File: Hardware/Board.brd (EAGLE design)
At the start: 170.2 x 111.2 mm, 103 parts, among them IC1 BD5229G-TR, IC4 XC6220A331MR-G, J1 FH34SRJ-24S-0.5SH_99_, J2 SAMACSYS_PARTS_USB4110-GF-A, J3 QWIIC_RIGHT_ANGLE, J4 112A-TAAR-R03_ATTEND, Q1 20V/4.2A/52mΩ/1.4W, Q2 20V/4.2A/52mΩ/1.4W, Q3 SI1308EDL-T1-GE3, U1 W25Q512JVEIQ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

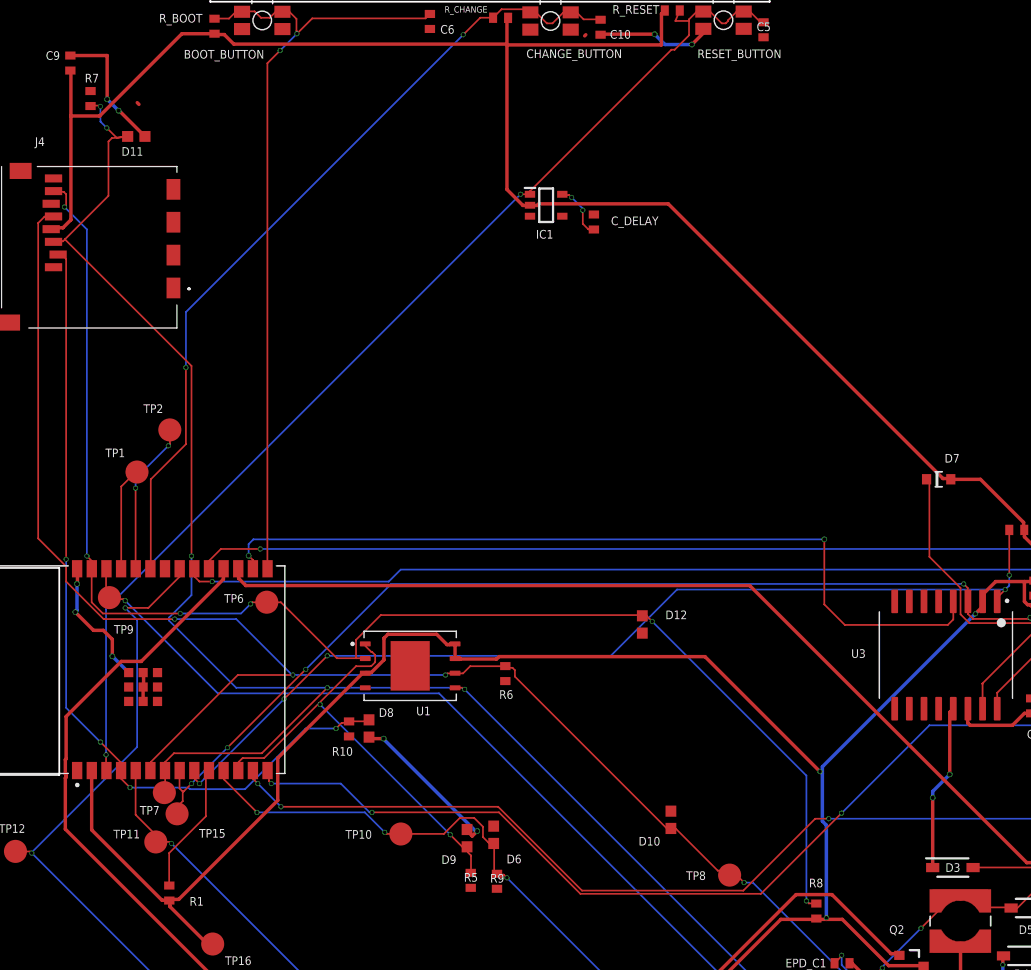
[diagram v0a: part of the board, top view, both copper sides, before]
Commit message: Remaining exploded view and manufacturing
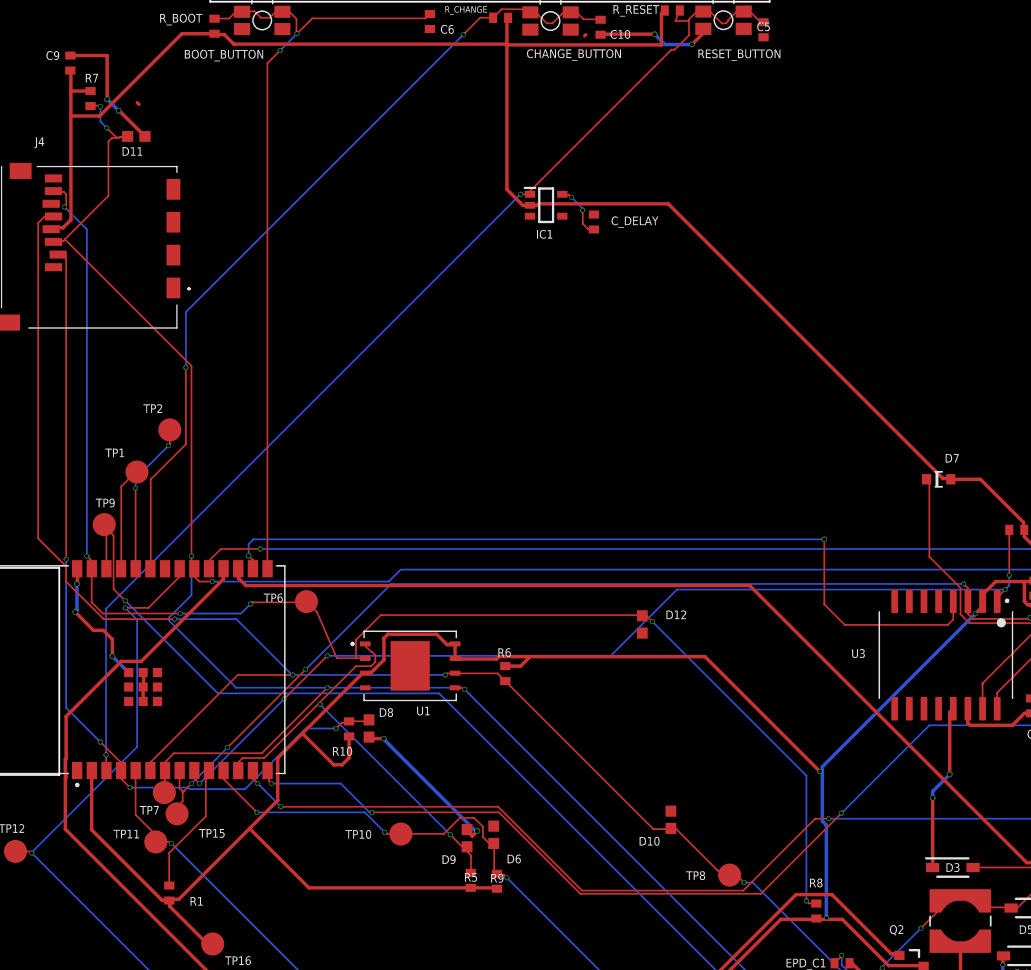
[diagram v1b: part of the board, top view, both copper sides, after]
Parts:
- R1: value (none) -> 10K
- moved TP9 6.35 mm to (10.3, 64.9)
- moved TP6 3.44 mm to (27.8, 58.2)
- turned R6 to 90 degrees
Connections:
- removed net N$26: R7.2
- removed net N$27: R6.2
- removed net N$28: R5.2
- removed net N$29: R9.2
- removed net N$30: R10.2
- net 3V3: now also R10.2, R5.2, R6.2, R7.2, R9.2
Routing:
- net 3V3: track 418.9 -> 454.0 mm
- net EPD_BUSY: track 99.3 -> 106.4 mm
- net MISO: track 123.3 -> 124.3 mm
- net SCK: track 148.0 -> 147.2 mm

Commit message: FInal version of files. Remaining gerbers
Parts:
- R_CHANGE: value (none) -> 10K
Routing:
- net GND: vias 18 -> 40
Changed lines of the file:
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@@
 <layer number="17" name="Pads" color="2" fill="1" visible="yes" active="yes"/>
 <layer number="18" name="Vias" color="2" fill="1" visible="yes" active="yes"/>
-<layer number="19" name="Unrouted" color="6" fill="1" visible="yes" active="yes"/>
+<layer number="19" name="Unrouted" color="6" fill="1" visible="no" active="yes"/>
 <layer number="20" name="Dimension" color="24" fill="1" visible="yes" active="yes"/>
 <layer number="21" name="tPlace" color="7" fill="1" visible="yes" active="yes"/>
@@
 <attribute name="VALUE" x="92.485" y="51.445" size="1.27" layer="27"/>
 </element>
-<element name="R_CHANGE" library="DeskAssistant v19 v1" library_urn="urn:adsk.wipprod:fs.file:vf.i3aUetO7RU6W5A7ASBjTVA" package="ESP32_WROVER_EAGLE-LTSPICE_R0402" package3d_urn="urn:adsk.eagle:package:47601124/1" value="" x="44.67" y="108.86" smashed="yes" rot="R179.6">
+<element name="R_CHANGE" library="DeskAssistant v19 v1" library_urn="urn:adsk.wipprod:fs.file:vf.i3aUetO7RU6W5A7ASBjTVA" package="ESP32_WROVER_EAGLE-LTSPICE_R0402" package3d_urn="urn:adsk.eagle:package:47601124/1" value="10K" x="44.67" y="108.86" smashed="yes" rot="R179.6">
 <attribute name="NAME" x="43.530553125" y="109.86058125" size="0.55" layer="21" rot="R180"/>
 <attribute name="SPICEMODEL" value="NONE" x="-38.40319375" y="216.12256875" size="1.778" layer="27" rot="R179.6" display="off"/>
@@
 <contactref element="C8" pad="2"/>
 <contactref element="C10_SUPERCAP" pad="1"/>
+<via x="59.77" y="107.55" extent="1-16" drill="0.35" alwaysstop="yes">
+</via>
+<via x="5.62" y="77.06" extent="1-16" drill="0.35" alwaysstop="yes">
+</via>
+<via x="82.77" y="67.26" extent="1-16" drill="0.35" alwaysstop="yes">
+</via>
+<via x="17.37" y="69.74" extent="1-16" drill="0.35" alwaysstop="yes">
+</via>
+<via x="18.36" y="58.67" extent="1-16" drill="0.35" alwaysstop="yes">
+</via>
+<via x="22.49" y="49.28" extent="1-16" drill="0.35" alwaysstop="yes">
+</via>
+<via x="25.11" y="47.86" extent="1-16" drill="0.35" alwaysstop="yes">
+</via>
+<via x="18.62" y="36.21" extent="1-16" drill="0.35" alwaysstop="yes">
+</via>
+<via x="24.15" y="41.07" extent="1-16" drill="0.35" alwaysstop="yes">
+</via>
+<via x="18.5" y="40.88" extent="1-16" drill="0.35" alwaysstop="yes">
+</via>
+<via x="13.34" y="59.16" extent="1-16" drill="0.35" alwaysstop="yes">
+</via>
+<via x="142.57" y="19.19" extent="1-16" drill="0.35" alwaysstop="yes">
+</via>
+<via x="145.89" y="45.7" extent="1-16" drill="0.35" alwaysstop="yes">
+</via>
+<via x="121.17" y="32.8" extent="1-16" drill="0.35" alwaysstop="yes">
+</via>
+<via x="126.18" y="37.27" extent="1-16" drill="0.35" alwaysstop="yes">
+</via>
+<via x="69.75" y="36.23" extent="1-16" drill="0.35" alwaysstop="yes">
+</via>
+<via x="70.66" y="14.19" extent="1-16" drill="0.35" alwaysstop="yes">
+</via>
+<via x="53.84" y="57.94" extent="1-16" drill="0.35" alwaysstop="yes">
+</via>
+<via x="55.84" y="35.13" extent="1-16" drill="0.35" alwaysstop="yes">
+</via>
+<via x="65.34" y="60.32" extent="1-16" drill="0.35" alwaysstop="yes">
+</via>
+<via x="75.7" y="15.67" extent="1-16" drill="0.35" alwaysstop="yes">
+</via>
+<via x="65.62" y="11.72" extent="1-16" drill="0.35" alwaysstop="yes">
+</via>
 </signal>
 <signal name="VBUS" class="1">
